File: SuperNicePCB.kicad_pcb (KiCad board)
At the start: 4 copper layers, 0 parts

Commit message: Changed footprint of the test point
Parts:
- added 3.1: TestPoint, TestPoint:TestPoint_Pad_1.0x1.0mm, F.Cu at (180.0, 110.0)
- added C1: 22uF, lcsc_footprints:C1859_C1206, F.Cu at (188.0, 91.5)
- added C10: 22uF, lcsc_footprints:C109448_C0603, F.Cu at (113.4, 124.2)
- added C11: 22uF, lcsc_footprints:C109448_C0603, F.Cu at (113.4, 126.9)
- added C12: 10nF, lcsc_footprints:C1589_C0603, F.Cu at (113.4, 129.6)
- added C13: 10uF, lcsc_footprints:C1713_C0805, F.Cu at (121.9, 135.3)
- added C14: 100nF, lcsc_footprints:C1525_C0402, F.Cu at (130.3, 99.4)
- added C15: 100nF, lcsc_footprints:C1525_C0402, F.Cu at (128.2, 88.8)
- added C16: 4,7uF, lcsc_footprints:C1705_C0603, F.Cu at (120.8, 77.3)
- added C17: 100nF, lcsc_footprints:C1525_C0402, F.Cu at (111.2, 80.9)
- added C18: 100n, lcsc_footprints:C1525_C0402, F.Cu at (177.5, 103.5)
- added C19: 100n, lcsc_footprints:C1525_C0402, F.Cu at (172.5, 111.8)
- added C2: 100nF, lcsc_footprints:C1525_C0402, F.Cu at (176.9, 85.9)
- added C20: 10u, lcsc_footprints:C1713_C0805, F.Cu at (182.0, 104.5)
- added C3: 100nF, lcsc_footprints:C1525_C0402, F.Cu at (176.9, 88.1)
- added C4: 1uF, lcsc_footprints:C1592_C0603, F.Cu at (177.5, 90.5)
- added C5: 22uF, lcsc_footprints:C109448_C0603, F.Cu at (113.4, 116.2)
- added C6: 10nF, lcsc_footprints:C1589_C0603, F.Cu at (113.4, 118.9)
- added C7: 10uF, lcsc_footprints:C1713_C0805, F.Cu at (121.9, 132.3)
- added C8: 22pF, lcsc_footprints:C76919_C0201, F.Cu at (126.4, 135.5)
- added C9: 10nF, lcsc_footprints:C1589_C0603, F.Cu at (113.4, 121.5)
- added GND1: TestPoint, TestPoint:TestPoint_Pad_1.0x1.0mm, F.Cu at (148.3, 115.3)
- added J1: UART Debug, Connector_PinHeader_1.27mm:PinHeader_1x04_P1.27mm_Vertical_SMD_Pin1Left, F.Cu at (180.0, 136.1)
- added J2: Boot Opt, Connector_PinHeader_1.27mm:PinHeader_1x02_P1.27mm_Vertical_SMD_Pin1Left, F.Cu at (179.0, 128.0)
- added J3: Signals Debug, Connector_PinHeader_1.27mm:PinHeader_2x12_P1.27mm_Vertical_SMD, F.Cu at (156.8, 134.2)
- added J4: GPIO Debug, Connector_PinHeader_1.27mm:PinHeader_2x06_P1.27mm_Vertical_SMD, F.Cu at (169.1, 135.8)
- added L1: 1.5uH, lcsc_footprints:C42100_IND-SMD_L4_0-W4_0, F.Cu at (128.0, 126.9)
- added LED1: 0603, lcsc_footprints:C2289_LED0603-RD, F.Cu at (173.1, 114.2)
- added LED2: APHD1608LCGCK, lcsc_footprints:C5139863_LED-SMD_L1_6-W0_8-RD_GREEN-1, F.Cu at (172.9, 116.8)
- added R1: 10k, lcsc_footprints:C1489_R1206, F.Cu at (188.0, 98.5)
- added R10: 10K, lcsc_footprints:C1489_R1206, F.Cu at (133.5, 88.5)
- added R11: 10K, lcsc_footprints:C1489_R1206, F.Cu at (133.5, 91.8)
- added R12: 100K, lcsc_footprints:C14675_R0603, F.Cu at (130.8, 97.1)
- added R13: 10K, lcsc_footprints:C1489_R1206, F.Cu at (127.4, 97.3)
- added R14: 10K, lcsc_footprints:C1489_R1206, F.Cu at (114.2, 74.5)
- added R15: 2K, lcsc_footprints:C4109_R0402, F.Cu at (101.2, 76.5)
- added R16: 2.7k, lcsc_footprints:C13167_R0603, F.Cu at (173.0, 94.9)
- added R17: 2.7k, lcsc_footprints:C13167_R0603, F.Cu at (173.0, 97.3)
- added R18: 100k, lcsc_footprints:C14675_R0603, F.Cu at (173.0, 99.8)
- added R2: 5.1K, lcsc_footprints:C14677_R0603, F.Cu at (117.4, 116.1)
- added R3: 5.1K, lcsc_footprints:C14677_R0603, F.Cu at (117.4, 118.6)
- added R4: 100k, lcsc_footprints:C14675_R0603, F.Cu at (117.4, 121.0)
- added R5: 90k, lcsc_footprints:C871504_R1206, F.Cu at (122.2, 125.9)
- added R6: 20K, lcsc_footprints:C4184_R0603, F.Cu at (117.4, 123.5)
- added R7: 100k, lcsc_footprints:C14675_R0603, F.Cu at (117.4, 126.0)
- added R8: 3.2K, lcsc_footprints:C705066_R0402, F.Cu at (131.2, 134.9)
- added R9: 10K, lcsc_footprints:C1489_R1206, F.Cu at (122.2, 129.2)
- added SW1: Reset, lcsc_footprints:C55200589_SW-SMD_4P-L4_2-W3_4-P2_15-LS5_2, F.Cu at (183.0, 85.0)
- added U1: ESP32-S3-WROOM-1-N8, lcsc_footprints:C2913198_WIFIM-SMD_ESP32-S3-WROOM-1-N8, F.Cu at (149.5, 68.9)
- added U2: SY8089AAAC, lcsc_footprints:C78988_SOT-23-5_L3_0-W1_7-P0_95-LS2_8-BR, F.Cu at (132.0, 131.7)
- added U3: SGM2048-ADJXTEK8G/TR, lcsc_footprints:C3294704_VDFN-8_L3_0-W3_0-P0_65-BL-EP, F.Cu at (127.4, 131.8)
- added U4: ICS-43434_C5656610, lcsc_footprints:C5656610_MIC-SMD_6P-L3_5-W2_7-P0_90-BL, F.Cu at (128.2, 93.3)
- added U5: AM312, lcsc_footprints:C114881_TO-5-3_L8_2-W8_2, F.Cu at (131.1, 82.8)
- added U6: SCD40-D-R1, lcsc_footprints:C3037696_LGA-20_L10_1-W10_1-P1_25-TL, F.Cu at (132.5, 70.3)
- added U7: SHT40-AD1B-R3, lcsc_footprints:C2848306_DFN-4_L1_5-W1_5-P0_8-TL-EP, F.Cu at (127.4, 100.1)
- added U8: HLK-LD6002, lcsc_footprints:C37897213_SENSOR-TH_HLK-LD6002, F.Cu at (101.2, 100.7)
- added U9: DWM3000TR13, lcsc_footprints:C5299931_WIRELM-SMD_DWM3000TR13, F.Cu at (160.6, 110.1)
- added USBC1: TYPE-C-31-M-12, lcsc_footprints:C165948_USB-C_SMD-TYPE-C-31-M-12_1, F.Cu at (112.5, 144.0)
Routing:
- net /MCU/VDD33: track 0.00 -> 3.93 mm
- net GND: track 0.00 -> 2.61 mm, vias 0 -> 2
- net Net-(USBC1-CC1): track 0.00 -> 2.11 mm
- net Net-(USBC1-CC2): track 0.00 -> 2.01 mm

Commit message: PCB layout for power
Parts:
- removed USBC1: TYPE-C-31-M-12, lcsc_footprints:C165948_USB-C_SMD-TYPE-C-31-M-12_1
- moved U9 46.4 mm to (179.1, 67.6)
- moved U8 28.3 mm to (113.0, 75.0), turned to 90 degrees
- moved U2 28.1 mm to (104.0, 129.7), turned to 90 degrees
- moved U1 27.5 mm to (150.0, 96.4)
- moved L1 26.8 mm to (101.5, 123.7), turned to 90 degrees
- moved R2 24.7 mm to (105.5, 137.8), turned to 90 degrees
- moved R3 24.6 mm to (102.0, 137.8), turned to 90 degrees
- moved R8 20.4 mm to (114.9, 122.5)
- moved C16 19.9 mm to (117.7, 97.0)
- moved R14 19.9 mm to (111.2, 94.2)
- moved R15 19.9 mm to (98.2, 96.2)
- moved C17 19.9 mm to (108.1, 100.5)
- moved R4 19.6 mm to (101.0, 131.7), turned to 90 degrees
- moved U6 19.2 mm to (149.7, 61.5)
- moved C5 19.1 mm to (103.8, 132.7)
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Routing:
- net Net-(U2-IN): track 0.00 -> 55.3 mm, vias 0 -> 3
- net GND: track 2.61 -> 38.9 mm, vias 2 -> 11
- net /MCU/VDD33: track 3.93 -> 25.8 mm, vias 0 -> 1
- net /HumanSesors/3.3V: track 0.00 -> 11.8 mm, vias 0 -> 1
- net /USB_D+: track 0.00 -> 8.09 mm, vias 0 -> 2
- net /USB_D-: track 0.00 -> 7.58 mm
- net Net-(U2-FB): track 0.00 -> 7.35 mm
- net Net-(U2-EN): track 0.00 -> 7.15 mm
- net Net-(U3-FB): track 0.00 -> 5.46 mm
- net Net-(U3-EN): track 0.00 -> 4.47 mm
- net Net-(U2-LX): track 0.00 -> 3.74 mm
- net Net-(U3-NR): track 0.00 -> 2.09 mm
- net Net-(USBC1-CC2): track 2.01 -> 3.11 mm
- net Net-(USBC1-CC1): track 2.11 -> 3.11 mm
- added copper zone on In1.Cu, net GND

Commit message: Beauty fixes
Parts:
- added USBC1: TYPE-C-31-M-12, lcsc_footprints:C165948_USB-C_SMD-TYPE-C-31-M-12_1, F.Cu at (103.4, 145.2)
- moved U9 5.59 mm to (173.6, 68.6)
- moved R3 0.50 mm to (101.5, 137.8)
- renumbered 3.1 to 3.3
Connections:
- C10 pad 1: /MCU/VDD33 -> /Power/+3.3V_Main
- C11 pad 1: /MCU/VDD33 -> /Power/+3.3V_Main
- C8 pad 1: /MCU/VDD33 -> /Power/+3.3V_Main
- L1 pad 2: /MCU/VDD33 -> /Power/+3.3V_Main
- R18 pad 1: /MCU/UWB_IRQ -> /UWB/UWB_IRQ
- R5 pad 1: /MCU/VDD33 -> /Power/+3.3V_Main
- U8 pad 7: /MCU/TXD -> /HumanSesors/R_TXO
- U8 pad 8: /MCU/RXD -> /HumanSesors/R_RX0
- U9 pad 15: /MCU/UWB_RXOK -> /UWB/UWB_RXOK
- U9 pad 17: /MCU/UWB_CS0 -> /UWB/UWB_CSn
- U9 pad 18: /MCU/UWB_MOSI -> /UWB/UWB_MOSI
- U9 pad 19: /MCU/UWB_MISO -> /UWB/UWB_MISO
- U9 pad 2: /MCU/UWB_WAKEUP -> /UWB/UWB_WAKE
- U9 pad 20: /MCU/UWB_SCK -> /UWB/UWB_CLK
- U9 pad 22: /MCU/UWB_IRQ -> /UWB/UWB_IRQ
- U9 pad 3: /MCU/UWB_RST -> /UWB/UWB_RSTn
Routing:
- net /USB_D-: track 7.58 -> 64.5 mm
- net /USB_D+: track 8.09 -> 63.4 mm
- net GND: track 38.9 -> 61.9 mm
- net /Power/+3.3V_Main: track 0.00 -> 21.9 mm, vias 0 -> 1
- net /MCU/VDD33: track 25.8 -> 3.93 mm, vias 1 -> 0
- net Net-(U2-IN): track 55.3 -> 58.0 mm
- net Net-(USBC1-CC1): track 3.11 -> 4.48 mm
- net Net-(USBC1-CC2): track 3.11 -> 4.33 mm
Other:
- board text added: "3V3 MCU"
- board text added: "3V3 sens"

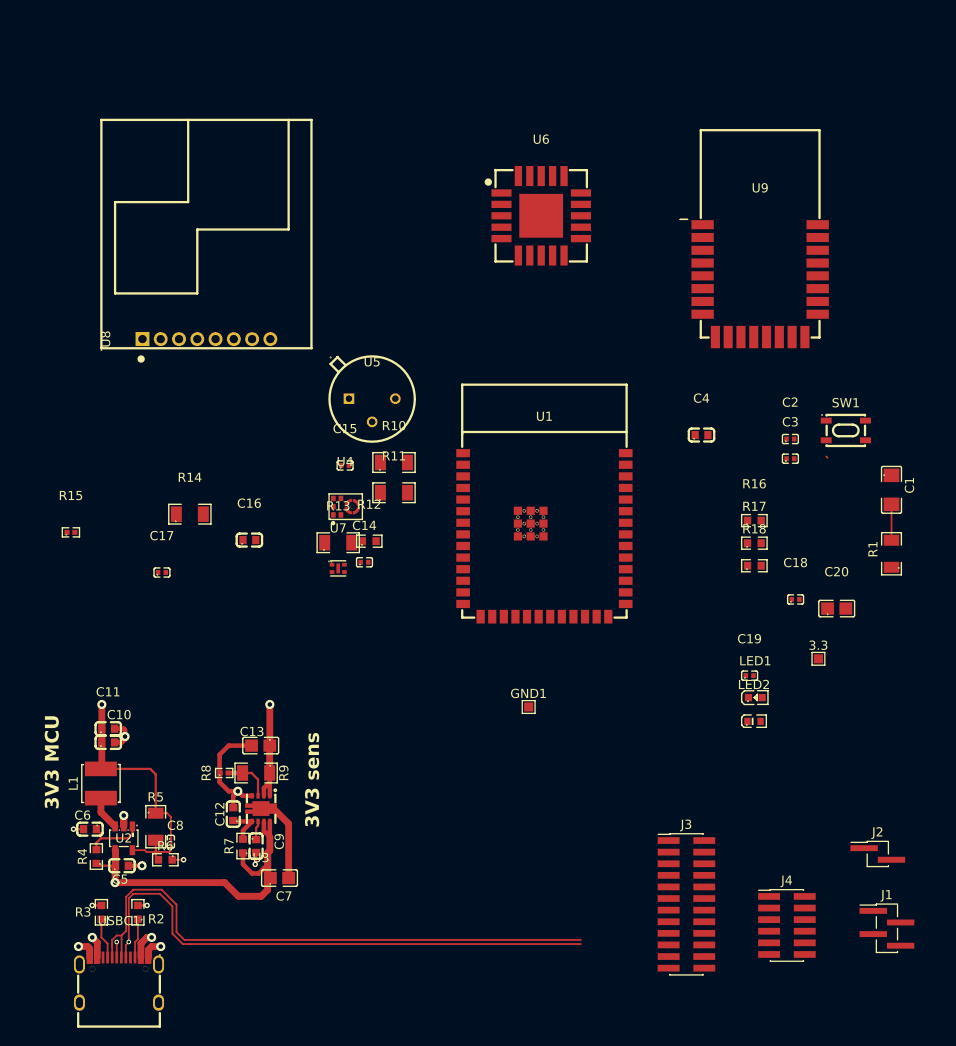
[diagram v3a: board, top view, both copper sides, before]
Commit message: placement rework of sensors and uwb, installation of power plane, starting of routing , UWB sheet net names aligned with MCU
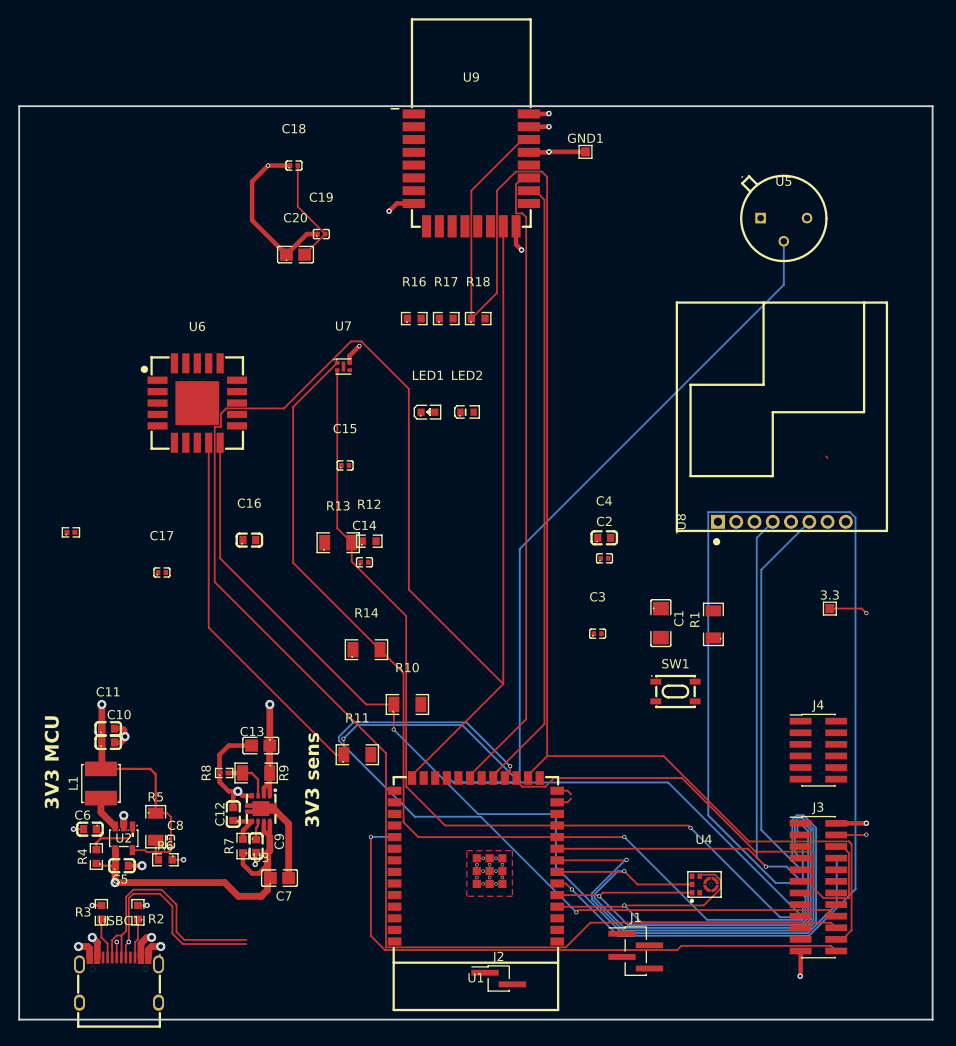
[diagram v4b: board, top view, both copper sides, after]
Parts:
- moved C18 72.6 mm to (122.6, 56.0)
- moved C20 70.8 mm to (122.8, 65.8)
- moved C19 67.3 mm to (125.6, 63.5)
- moved U8 66.1 mm to (176.0, 95.0)
- moved GND1 61.1 mm to (154.5, 54.5)
- moved U4 57.0 mm to (167.5, 134.7)
- moved U5 49.2 mm to (176.2, 63.0)
- moved LED1 47.5 mm to (137.2, 83.0)
- moved LED2 46.2 mm to (141.5, 83.0)
- moved J2 43.7 mm to (145.0, 145.0)
- moved R16 43.3 mm to (135.8, 72.8)
- moved U6 42.9 mm to (112.0, 82.0)
- moved R17 41.7 mm to (139.2, 72.8)
- moved R18 40.6 mm to (142.8, 72.8)
- moved U1 36.3 mm to (142.5, 132.0), turned to 180 degrees
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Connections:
- net /UWB/UWB_CLK renamed /UWB/UWB_SCK
- net /UWB/UWB_CSn renamed /UWB/UWB_CS0
- net /UWB/UWB_RSTn renamed /UWB/UWB_RST
- net /UWB/UWB_WAKE renamed /UWB/UWB_WAKEUP
- C10 pad 1: /Power/+3.3V_Main -> /MCU/VDD33
- C11 pad 1: /Power/+3.3V_Main -> /MCU/VDD33
- C8 pad 1: /Power/+3.3V_Main -> /MCU/VDD33
- L1 pad 2: /Power/+3.3V_Main -> /MCU/VDD33
- R18 pad 1: /UWB/UWB_IRQ -> /MCU/UWB_IRQ
- R5 pad 1: /Power/+3.3V_Main -> /MCU/VDD33
- U8 pad 7: /HumanSesors/R_TXO -> /MCU/TXD
- U8 pad 8: /HumanSesors/R_RX0 -> /MCU/RXD
- U9 pad 15: /UWB/UWB_RXOK -> /MCU/UWB_RXOK
- U9 pad 18: /UWB/UWB_MOSI -> /MCU/UWB_MOSI
- U9 pad 19: /UWB/UWB_MISO -> /MCU/UWB_MISO
- U9 pad 22: /UWB/UWB_IRQ -> /MCU/UWB_IRQ
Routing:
- net /MCU/UWB_RXOK: track 0.00 -> 245.0 mm
- net /MCU/UWB_IRQ: track 0.00 -> 159.9 mm
- net /MCU/AC_DOUT: track 0.00 -> 144.9 mm, vias 0 -> 1
- net /PIR_OUT: track 0.00 -> 123.5 mm
- net /HumanSesors/CO2_SCL: track 0.00 -> 116.4 mm, vias 0 -> 1
- net /TEMP_SDA: track 0.00 -> 109.7 mm, vias 0 -> 1
- net /HumanSesors/C02_SDA: track 0.00 -> 108.6 mm, vias 0 -> 1
- net /HumanSesors/U0_RTS: track 0.00 -> 100.0 mm, vias 0 -> 1
- net /TEMP_SCL: track 0.00 -> 99.3 mm, vias 0 -> 1
- net /MCU/UWB_CS0: track 0.00 -> 86.0 mm, vias 0 -> 2
- net /MCU/UWB_MISO: track 0.00 -> 70.8 mm
- net /MCU/UWB_MOSI: track 0.00 -> 69.7 mm
- net /HumanSesors/U0_CTS: track 0.00 -> 66.9 mm, vias 0 -> 1
- net /MCU/UWB_RST: track 0.00 -> 65.3 mm, vias 0 -> 1
- net /HumanSesors/DIN: track 0.00 -> 62.6 mm, vias 0 -> 1
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- added copper zone on In2.Cu, net /HumanSesors/3.3V
- added copper zone on F.Cu, net GND
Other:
- board outline added: 100 x 100 mm

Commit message: KiCad: PCB placement, routing and schematic updates
Wiring of component blocks and sensors + component rearrangement + routing
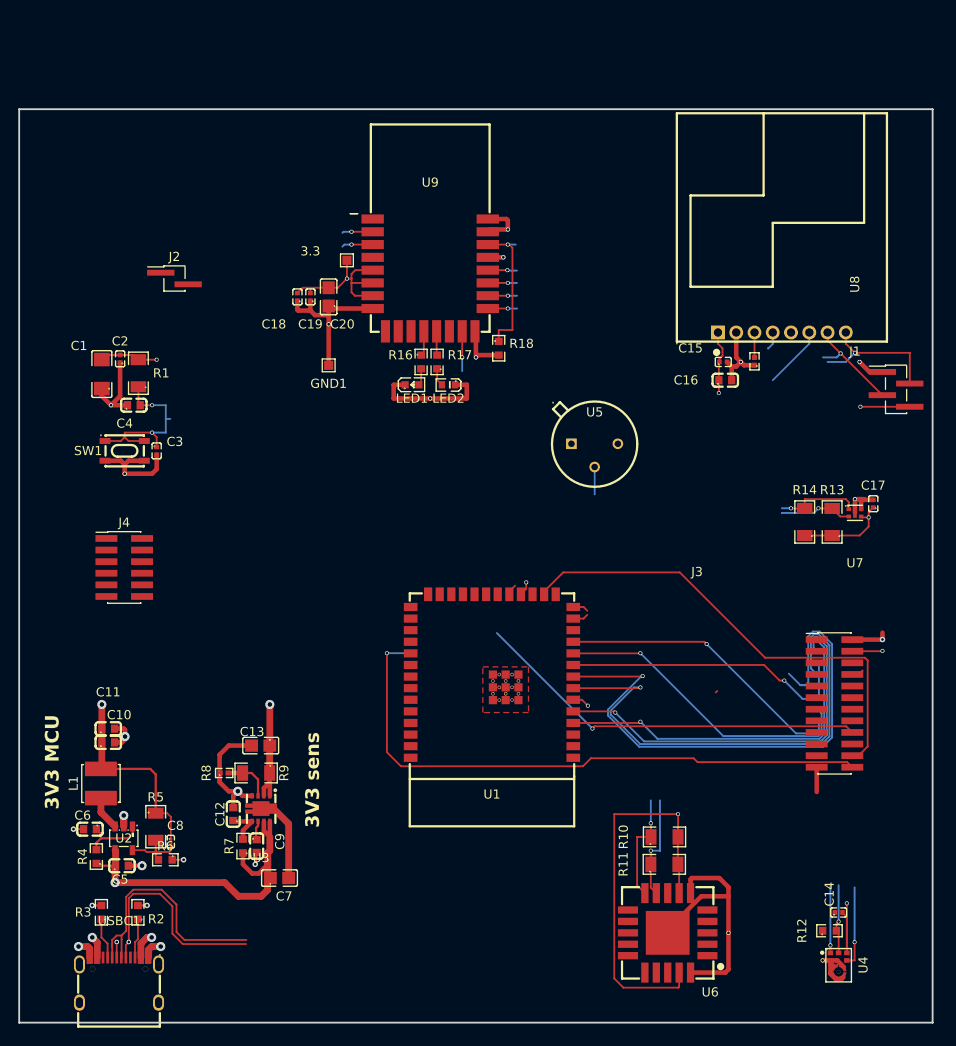
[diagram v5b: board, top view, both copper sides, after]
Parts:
- moved J2 84.5 mm to (109.5, 68.4)
- moved J4 78.6 mm to (104.0, 100.0)
- moved C17 78.2 mm to (186.0, 93.0), turned to 90 degrees
- moved U6 77.6 mm to (163.5, 140.0), turned to 180 degrees
- moved R15 77.1 mm to (173.0, 77.4), turned to 90 degrees
- moved R1 68.7 mm to (105.5, 78.7)
- moved J1 67.8 mm to (188.5, 80.5)
- moved C1 67.0 mm to (101.5, 78.8), turned to 90 degrees
- moved R12 66.0 mm to (181.2, 139.8)
- moved SW1 65.8 mm to (104.0, 87.2)
- moved 3.3 65.2 mm to (128.4, 66.4)
- moved C14 64.5 mm to (182.2, 137.8)
- moved U7 58.2 mm to (184.0, 94.0)
- moved C2 57.4 mm to (103.5, 77.2), turned to 90 degrees
- moved C16 55.0 mm to (169.8, 79.5)
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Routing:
- net /MCU/UWB_RXOK: track 245.0 -> 4.96 mm, vias 0 -> 1
- net GND: track 105.6 -> 257.9 mm, vias 20 -> 24
- net /MCU/AC_DOUT: track 144.9 -> 6.10 mm
- net /PIR_OUT: track 123.5 -> 3.37 mm
- net /HumanSesors/CO2_SCL: track 116.4 -> 12.4 mm
- net /HumanSesors/C02_SDA: track 108.6 -> 13.4 mm
- net /HumanSesors/3.3V: track 27.9 -> 119.6 mm, vias 2 -> 6
- net /MCU/UWB_IRQ: track 159.9 -> 68.3 mm, vias 0 -> 1
- net /MCU/UWB_MISO: track 70.8 -> 4.20 mm, vias 0 -> 1
- net /TEMP_SDA: track 109.7 -> 44.2 mm, vias 1 -> 2
- net /MCU/UWB_MOSI: track 69.7 -> 4.70 mm, vias 0 -> 1
- net /TEMP_SCL: track 99.3 -> 40.2 mm, vias 1 -> 2
- net /MCU/UWB_CS0: track 86.0 -> 45.2 mm
- net /HumanSesors/U0_CTS: track 66.9 -> 29.9 mm
- net /HumanSesors/U0_RTS: track 100.0 -> 70.1 mm
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
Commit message: Data lines layout. Missing power lines and UWB
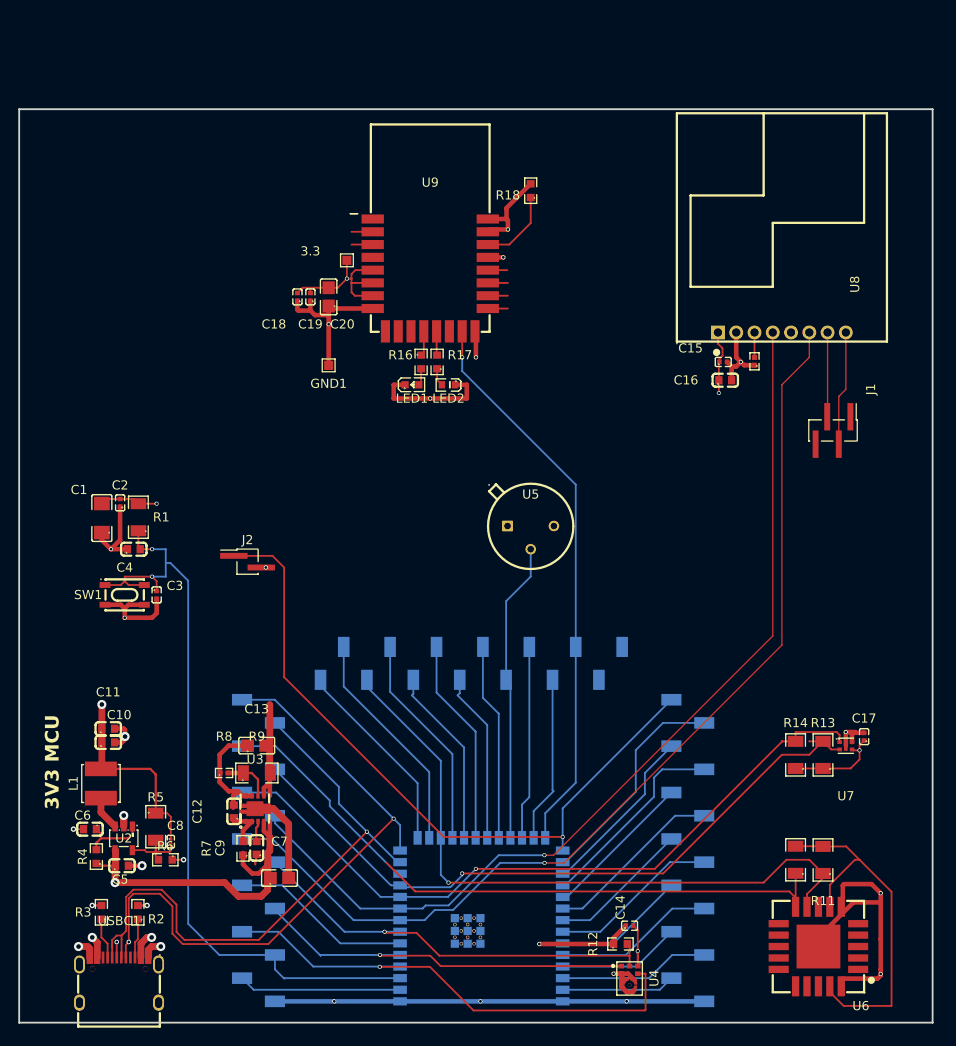
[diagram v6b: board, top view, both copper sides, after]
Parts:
- removed J3: Signals Debug, Connector_PinHeader_1.27mm:PinHeader_2x12_P1.27mm_Vertical_SMD
- removed J4: GPIO Debug, Connector_PinHeader_1.27mm:PinHeader_2x06_P1.27mm_Vertical_SMD
- added H1: 1010301753, lcsc_footprints:C52016809_HDR-SMD_14P-P2_54-V-M-S4_8, B.Cu at (118.7, 131.0)
- added H2: 1010301753, lcsc_footprints:C52016809_HDR-SMD_14P-P2_54-V-M-S4_8, B.Cu at (142.0, 110.5)
- added H3: 1010301753, lcsc_footprints:C52016809_HDR-SMD_14P-P2_54-V-M-S4_8, B.Cu at (165.7, 131.0)
- U1: moved to B.Cu
- moved J2 32.0 mm to (117.5, 99.4)
- moved U1 26.7 mm to (143.1, 138.6), turned to 0 degrees
- moved C17 25.5 mm to (185.0, 118.5)
- moved R13 25.5 mm to (180.5, 120.5)
- moved R14 25.5 mm to (177.5, 120.5)
- moved U7 25.5 mm to (183.0, 119.5)
- moved C14 22.9 mm to (159.3, 139.2)
- moved R12 22.9 mm to (158.3, 141.2)
- moved U4 22.9 mm to (159.3, 144.9)
- moved R18 17.6 mm to (148.5, 58.8), turned to 90 degrees
- moved R11 17.4 mm to (180.5, 132.0), turned to 90 degrees
- moved U6 16.6 mm to (180.0, 141.5)
- moved C1 15.8 mm to (101.5, 94.6)
- moved C2 15.8 mm to (103.5, 92.9)
- moved C3 15.8 mm to (107.5, 103.0)
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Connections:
- U1 pad 2: /MCU/VDD33 -> Net-(U1-3V3)
- U1 pad 36: /MCU/RXD -> Net-(U1-RXD0)
- U1 pad 37: /MCU/TXD -> Net-(U1-TXD0)
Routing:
- net /MCU/BOOT: track 0.00 -> 77.2 mm, vias 0 -> 1
- net /HumanSesors/U0_CTS: track 29.9 -> 104.8 mm
- net /MCU/EN: track 19.8 -> 86.8 mm
- net /HumanSesors/CO2_SCL: track 12.4 -> 73.1 mm
- net /HumanSesors/C02_SDA: track 13.4 -> 73.9 mm, vias 1 -> 0
- net GND: track 257.9 -> 318.3 mm, vias 24 -> 26
- net /MCU/UWB_RXOK: track 4.96 -> 62.0 mm
- net /MCU/UWB_RST: track 65.7 -> 16.6 mm, vias 1 -> 0
- net /USB_D+: track 28.4 -> 74.3 mm, vias 2 -> 3
- net /HumanSesors/U0_RTS: track 70.1 -> 110.7 mm
- net /USB_D-: track 29.6 -> 67.0 mm, vias 0 -> 1
- net /TEMP_SCL: track 40.2 -> 75.8 mm, vias 2 -> 1
- net /TEMP_SDA: track 44.2 -> 79.2 mm, vias 2 -> 1
- net /MCU/UWB_IRQ: track 68.3 -> 34.0 mm, vias 1 -> 0
- net /PIR_OUT: track 3.37 -> 32.9 mm
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- removed copper zone on F.Cu, net GND
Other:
- board text removed: "3V3 sens"
